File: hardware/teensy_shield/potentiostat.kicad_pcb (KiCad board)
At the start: 2 copper layers, 144.8 x 88.9 mm, 98 parts, among them K1 CONN_3, P1 CONN_2, P10 CONN_2, P11 CONN_2, P12 CONN_2, P13 CONN_5X2, P14 CONN_5X2, P15 CONN_2X2, P16 CONN_2X2, P17 CONN_2, P18 CONN_2, P19 CONN_2, P2 CONN_2, P20 CONN_2, P21 CONN_2, P3 CONN_2, P4 CONN_2, P5 CONN_2, P6 CONN_2, P7 CONN_2, P8 CONN_2, P9 CONN_2, U1 ZXRE060, U10 OPA227, U11 OP07, U12 LT1995, U13 ADG44X, U2 TEENSY3.1, U3 MAX6176AASA+, U4 LT1995, U5 AD8250, U6 MEA1D05XXSC, U7 OPA129, U8 OPA129, U9 ADG44X

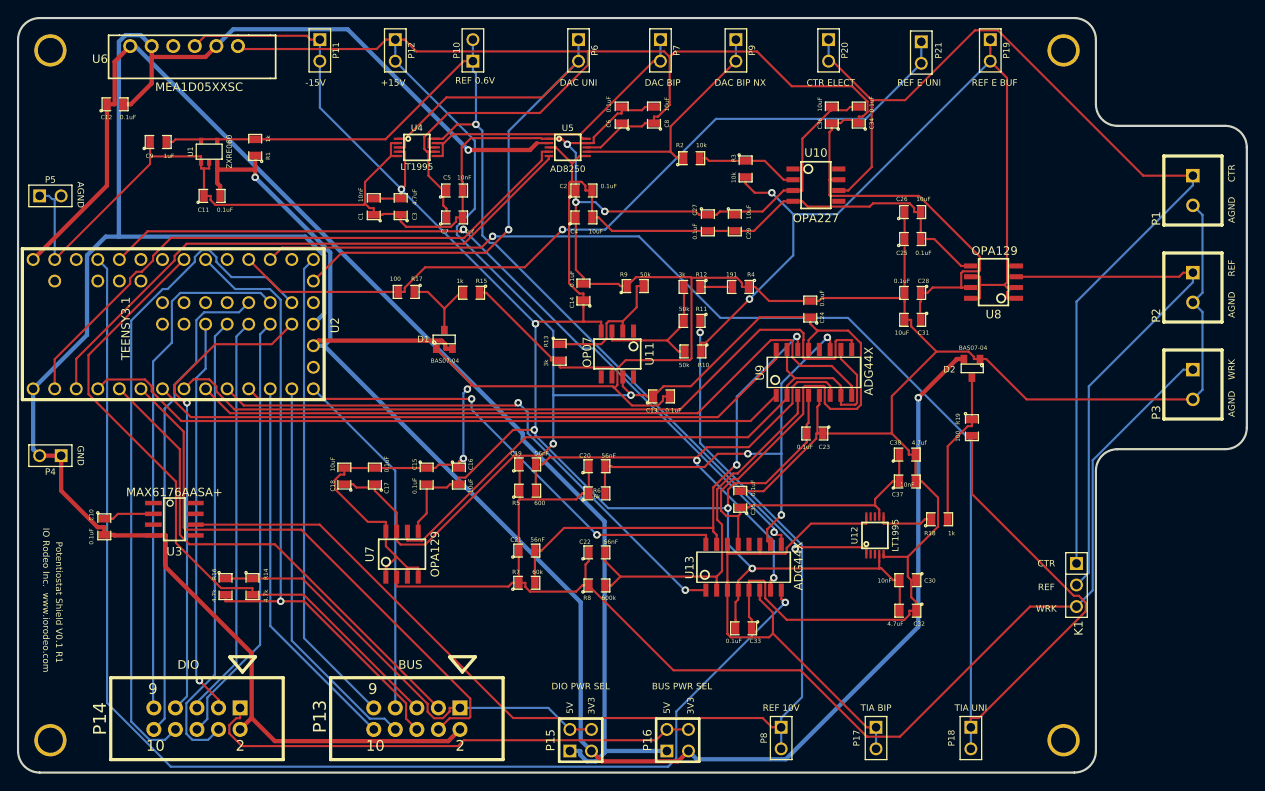
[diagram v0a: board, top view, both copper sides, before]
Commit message: Cleaned up silkscreen and created gerber files.
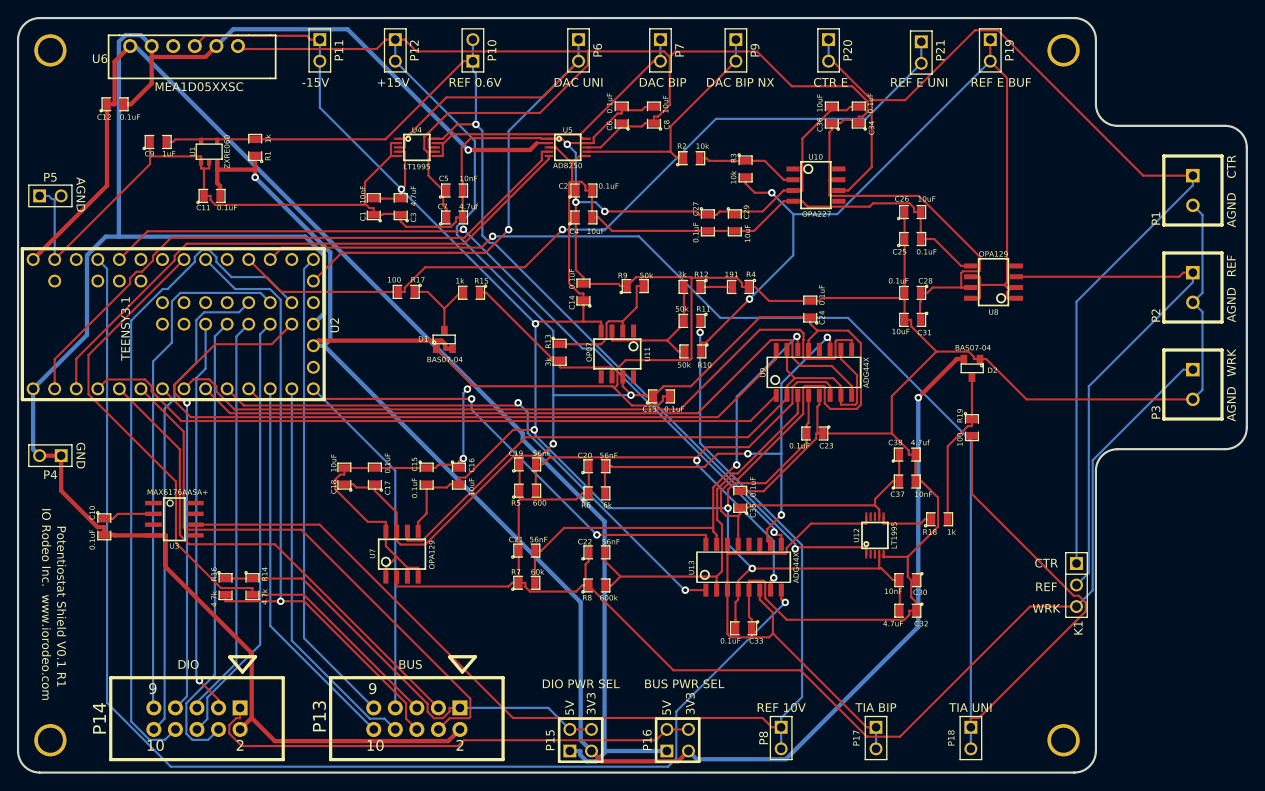
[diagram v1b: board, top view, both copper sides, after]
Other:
- board text added: "CTR E"
- board text removed: "CTR ELECT"

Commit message: Fixed issues schematic. Added new parts to layout. Updated BOM. Board not yet re-routed.
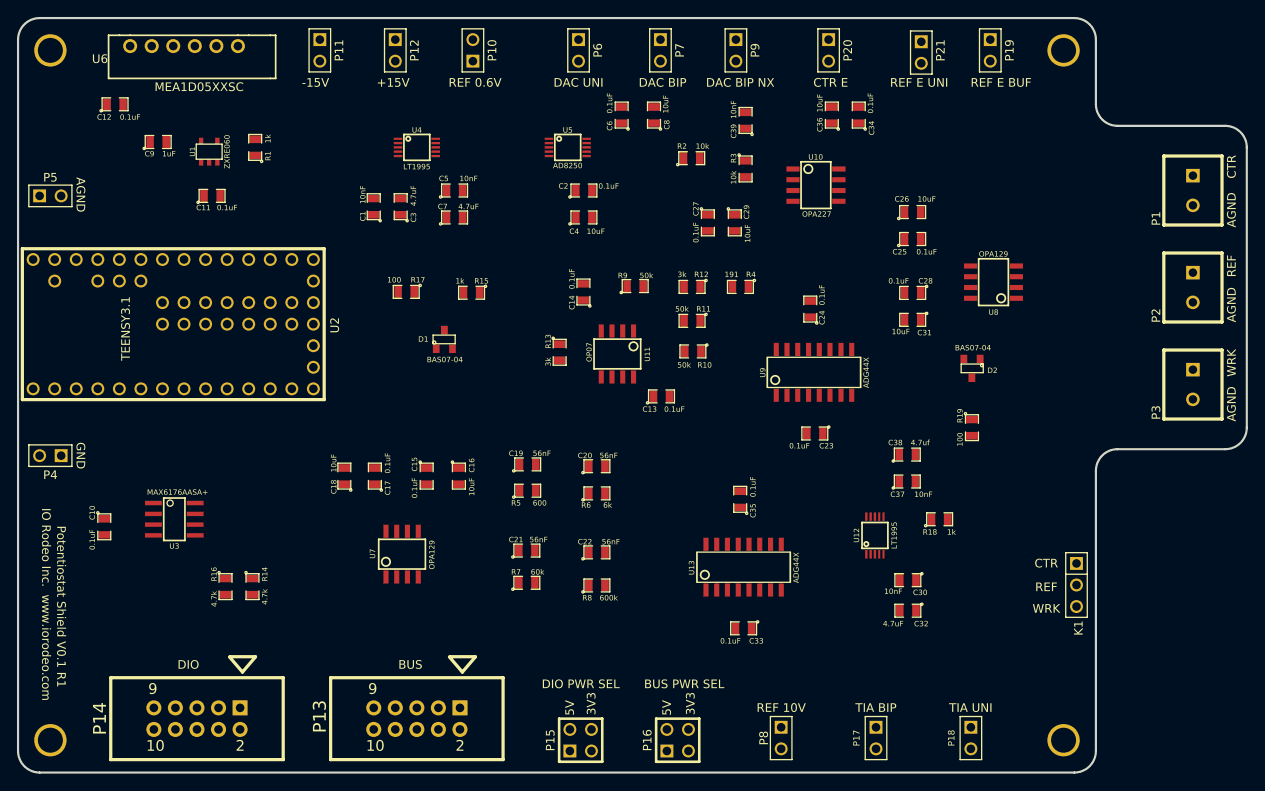
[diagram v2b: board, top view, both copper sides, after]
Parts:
- added C39: 10nF, SM0805, F.Cu at (136.5, 62.9)
- C7: value 4.7uf -> 4.7uF
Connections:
- C10 pad 1: /15V -> /+15V
- U3 pad 2: /15V -> /+15V
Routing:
- net /AGND: track 493.9 -> 0.00 mm, vias 5 -> 0
- net /+15V: track 391.7 -> 0.00 mm, vias 2 -> 0
- net /-15V: track 282.5 -> 0.00 mm, vias 5 -> 0
- net /GND: track 231.4 -> 0.00 mm, vias 1 -> 0
- net /3V3: track 195.0 -> 0.00 mm, vias 2 -> 0
- net /TIA_OUT_UNI: track 176.4 -> 0.00 mm, vias 1 -> 0
- net /WRK_ELECT: track 160.1 -> 0.00 mm
- net /5V: track 149.8 -> 0.00 mm
- net /TIA_SW2_IN4: track 148.7 -> 0.00 mm, vias 1 -> 0
- net /REF_10V: track 135.3 -> 0.00 mm, vias 1 -> 0
- net /REF_0V6: track 133.9 -> 0.00 mm, vias 2 -> 0
- net /CTR_ELECT: track 122.1 -> 0.00 mm
- net /REF_ELECT_BUF: track 102.3 -> 0.00 mm, vias 2 -> 0
- net /TIA_SW2_IN3: track 95.8 -> 0.00 mm, vias 2 -> 0
- net /REF_ELECT_UNI: track 94.8 -> 0.00 mm, vias 1 -> 0
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
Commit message: Re-routed board and created new gerber files.
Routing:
- net /AGND: track 0.00 -> 563.5 mm, vias 0 -> 3
- net /+15V: track 0.00 -> 373.5 mm, vias 0 -> 2
- net /-15V: track 0.00 -> 301.1 mm, vias 0 -> 5
- net /GND: track 0.00 -> 229.1 mm, vias 0 -> 1
- net /3V3: track 0.00 -> 194.9 mm, vias 0 -> 1
- net /WRK_ELECT: track 0.00 -> 166.7 mm
- net /5V: track 0.00 -> 156.8 mm
- net /TIA_OUT_UNI: track 0.00 -> 155.7 mm
- net /REF_0V6: track 0.00 -> 140.1 mm, vias 0 -> 1
- net /REF_10V: track 0.00 -> 135.0 mm, vias 0 -> 1
- net /CTR_ELECT: track 0.00 -> 132.8 mm
- net /SCL: track 0.00 -> 129.9 mm
- net /TIA_SW2_IN4: track 0.00 -> 105.7 mm, vias 0 -> 1
- net /TIA_SW2_IN3: track 0.00 -> 103.1 mm, vias 0 -> 1
- net /REF_ELECT_BUF: track 0.00 -> 100.9 mm, vias 0 -> 2
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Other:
- board text added: "Potentiostat Shield V0.1 R2"
- board text removed: "Potentiostat Shield V0.1 R1"
